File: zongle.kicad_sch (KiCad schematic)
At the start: 20 parts, among them U1 453-00059R

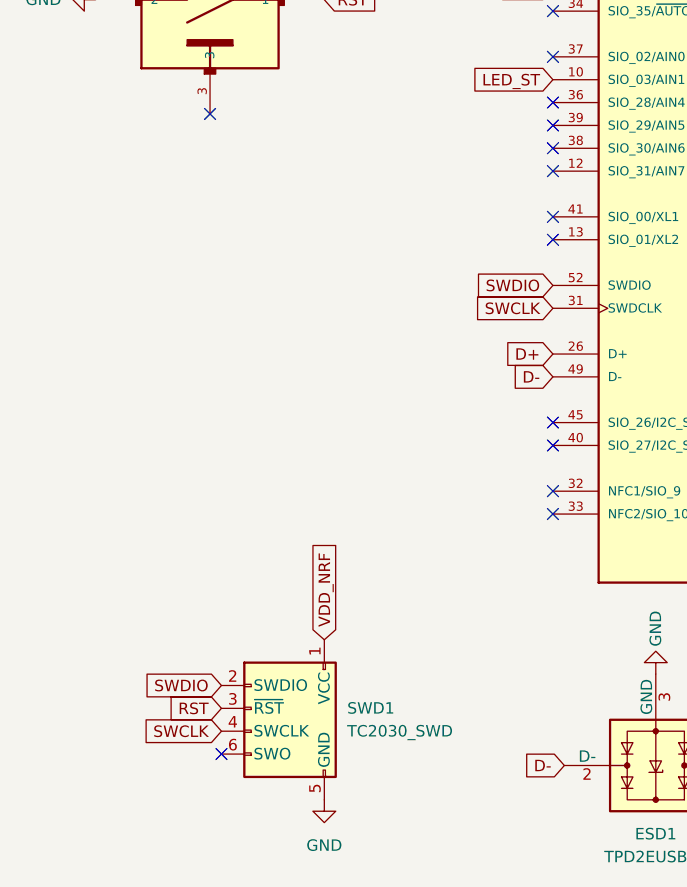
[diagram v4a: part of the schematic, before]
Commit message: some routing cleanup, some drc fixes, assigned parts to every footprint
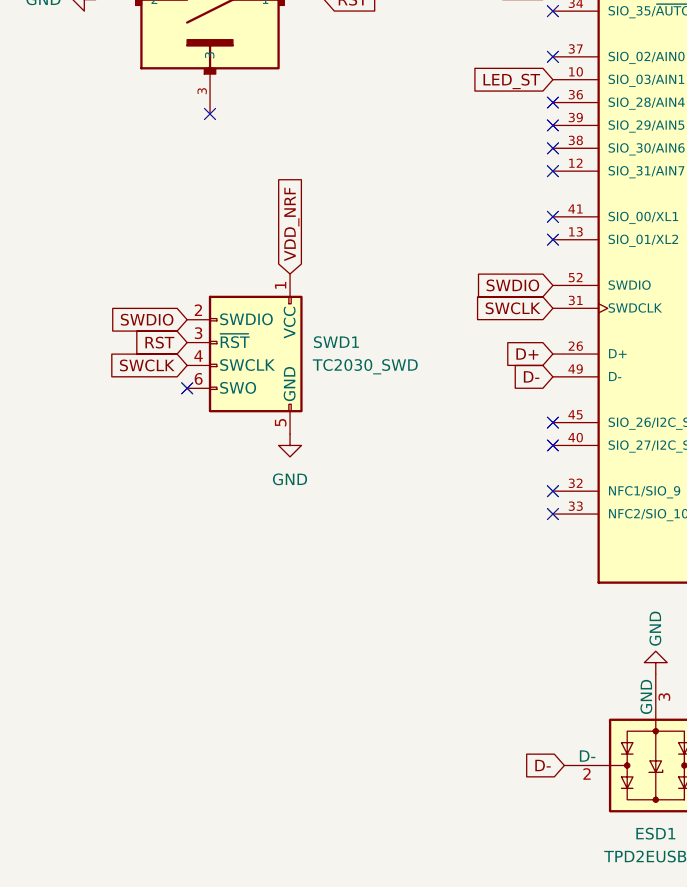
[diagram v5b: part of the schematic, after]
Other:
- moved on the sheet: SWD1
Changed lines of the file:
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@@
 	)
 	(no_connect
-		(at 34.29 149.86)
+		(at 30.48 109.22)
 	)
 	(no_connect
@@
 	(global_label "RST"
 		(shape input)
-		(at 34.29 144.78 180)
-		(fields_autoplaced yes)
-		(effects
-			(font
-				(size 1.27 1.27)
-			)
-			(justify right)
-		)
-		(property "Intersheetrefs" "${INTERSHEET_REFS}"
-			(at 27.8577 144.78 0)
+		(at 30.48 104.14 180)
+		(fields_autoplaced yes)
+		(effects
+			(font
+				(size 1.27 1.27)
+			)
+			(justify right)
+		)
+		(property "Intersheetrefs" "${INTERSHEET_REFS}"
+			(at 24.0477 104.14 0)
 			(effects
 				(font
@@
 	(global_label "SWCLK"
 		(shape input)
-		(at 34.29 147.32 180)
-		(fields_autoplaced yes)
-		(effects
-			(font
-				(size 1.27 1.27)
-			)
-			(justify right)
-		)
-		(property "Intersheetrefs" "${INTERSHEET_REFS}"
-			(at 25.0758 147.32 0)
+		(at 30.48 106.68 180)
+		(fields_autoplaced yes)
+		(effects
+			(font
+				(size 1.27 1.27)
+			)
+			(justify right)
+		)
+		(property "Intersheetrefs" "${INTERSHEET_REFS}"
+			(at 21.2658 106.68 0)
 			(effects
 				(font
@@
 	(global_label "VDD_NRF"
 		(shape input)
-		(at 45.72 137.16 90)
+		(at 41.91 96.52 90)
 		(fields_autoplaced yes)
 		(effects
@@
 		)
 		(property "Intersheetrefs" "${INTERSHEET_REFS}"
-			(at 45.72 125.8895 90)
+			(at 41.91 85.2495 90)
 			(effects
 				(font
@@
 	(global_label "SWDIO"
 		(shape input)
-		(at 34.29 142.24 180)
-		(fields_autoplaced yes)
-		(effects
-			(font
-				(size 1.27 1.27)
-			)
-			(justify right)
-		)
-		(property "Intersheetrefs" "${INTERSHEET_REFS}"
-			(at 25.4386 142.24 0)
+		(at 30.48 101.6 180)
+		(fields_autoplaced yes)
+		(effects
+			(font
+				(size 1.27 1.27)
+			)
+			(justify right)
+		)
+		(property "Intersheetrefs" "${INTERSHEET_REFS}"
+			(at 21.6286 101.6 0)
 			(effects
 				(font
@@
 	(symbol
 		(lib_id "marbastlib-various:TC2030_SWD")
-		(at 40.64 147.32 0)
+		(at 36.83 106.68 0)
 		(unit 1)
 		(exclude_from_sim no)
@@
 		(fields_autoplaced yes)
 		(property "Reference" "SWD1"
-			(at 48.26 144.7799 0)
+			(at 44.45 104.1399 0)
 			(effects
 				(font
@@
 		)
 		(property "Value" "TC2030_SWD"
-			(at 48.26 147.3199 0)
+			(at 44.45 106.6799 0)
 			(effects
 				(font
@@
 		)
 		(property "Footprint" "marbastlib-various:CON_TC2030_outlined"
-			(at 50.8 146.05 90)
+			(at 46.99 105.41 90)
 			(effects
 				(font
@@
 		)
 		(property "Datasheet" "~"
-			(at 8.255 161.29 0)
+			(at 4.445 120.65 0)
 			(effects
 				(font
@@
 		)
 		(property "Description" "6-pin TC2030 connector for SWD programming"
-			(at 40.64 147.32 0)
+			(at 36.83 106.68 0)
 			(effects
 				(font
@@
 	(symbol
 		(lib_id "power:GND")
-		(at 45.72 154.94 0)
+		(at 41.91 114.3 0)
 		(unit 1)
 		(exclude_from_sim no)
@@
 		(fields_autoplaced yes)
 		(property "Reference" "#PWR07"
-			(at 45.72 161.29 0)
+			(at 41.91 120.65 0)
 			(effects
 				(font
@@
 		)
 		(property "Value" "GND"
-			(at 45.72 160.02 0)
+			(at 41.91 119.38 0)
 			(effects
 				(font
@@
 		)
 		(property "Footprint" ""
-			(at 45.72 154.94 0)
+			(at 41.91 114.3 0)
 			(effects
 				(font
@@
 		)
 		(property "Datasheet" ""
-			(at 45.72 154.94 0)
+			(at 41.91 114.3 0)
 			(effects
 				(font
@@
 		)
 		(property "Description" "Power symbol creates a global label with name \"GND\" , ground"
-			(at 45.72 154.94 0)
-			(effects
-				(font
+			(at 41.91 114.3 0)
+			(effects
+				(font

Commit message: minor changes to the routing. final tweaks for first version
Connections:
- no-connect marks 44 -> 43
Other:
- moved on the sheet: C22, C26, ESD1, F1, FB1, LED_STATUS1, R21, R23, R26, SWD1, SWReset_1, Tp+5v1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

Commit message: linked model for 453-00059 nrf52833 module, later will move all the modules to the project repo, so that using this on another device is possible without new linking of the models
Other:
- title: (none) -> zongle
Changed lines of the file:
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@@
 	(generator_version "9.0")
 	(paper "A4")
+	(title_block
+		(title "zongle")
+		(date "2025-12-10")
+		(rev "0.0.2")
+	)
 	(junction
 		(at 185.42 123.19)

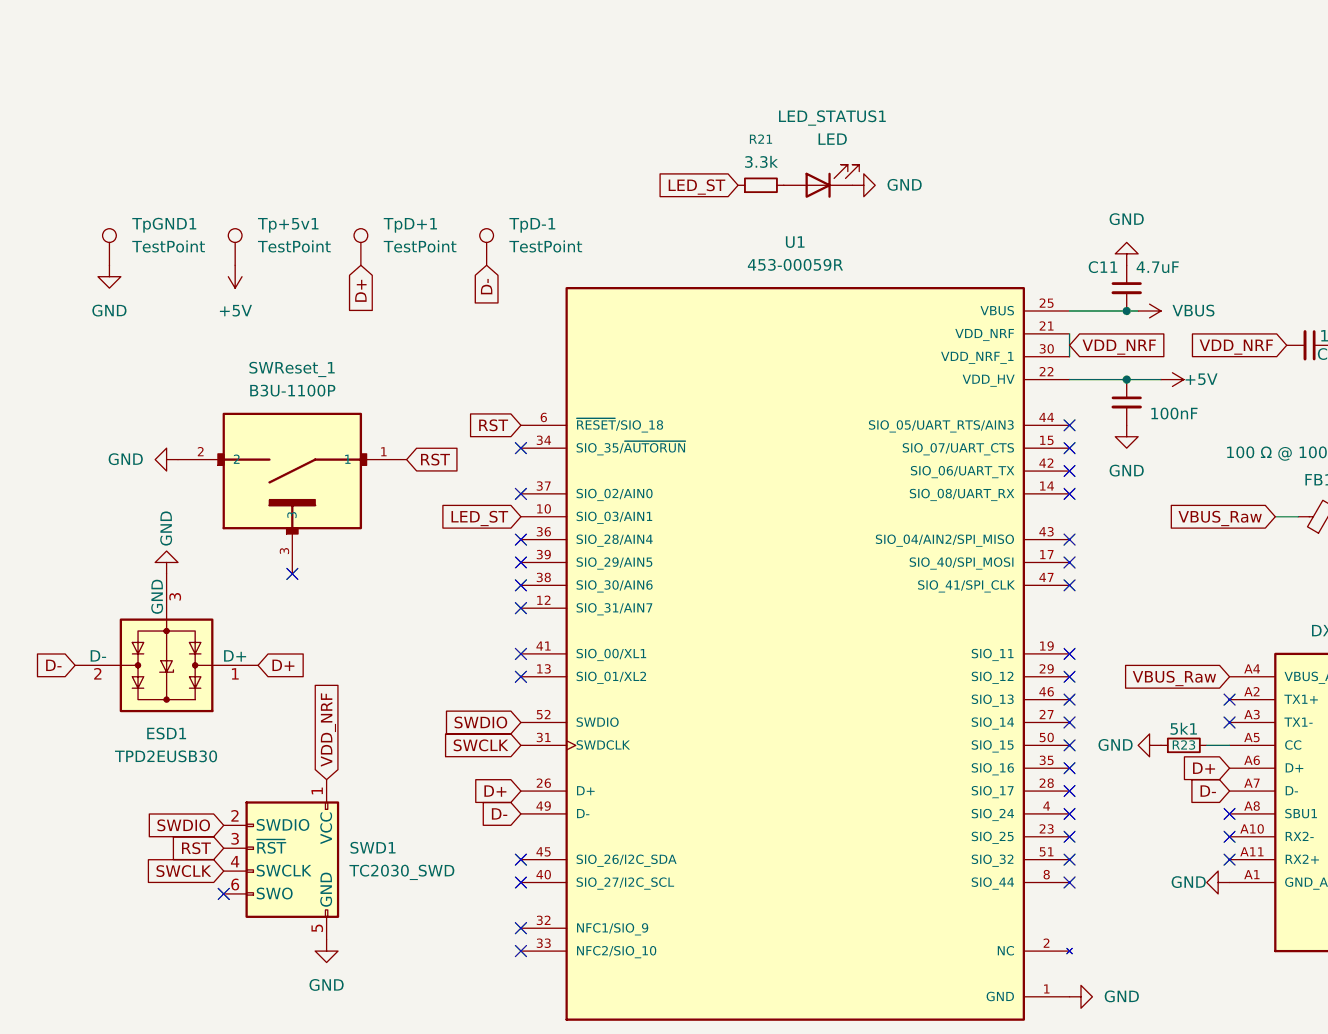
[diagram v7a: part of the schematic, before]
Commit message: moved led outside of antenna perimeter just to be extra sure. some via stitching + cleanup
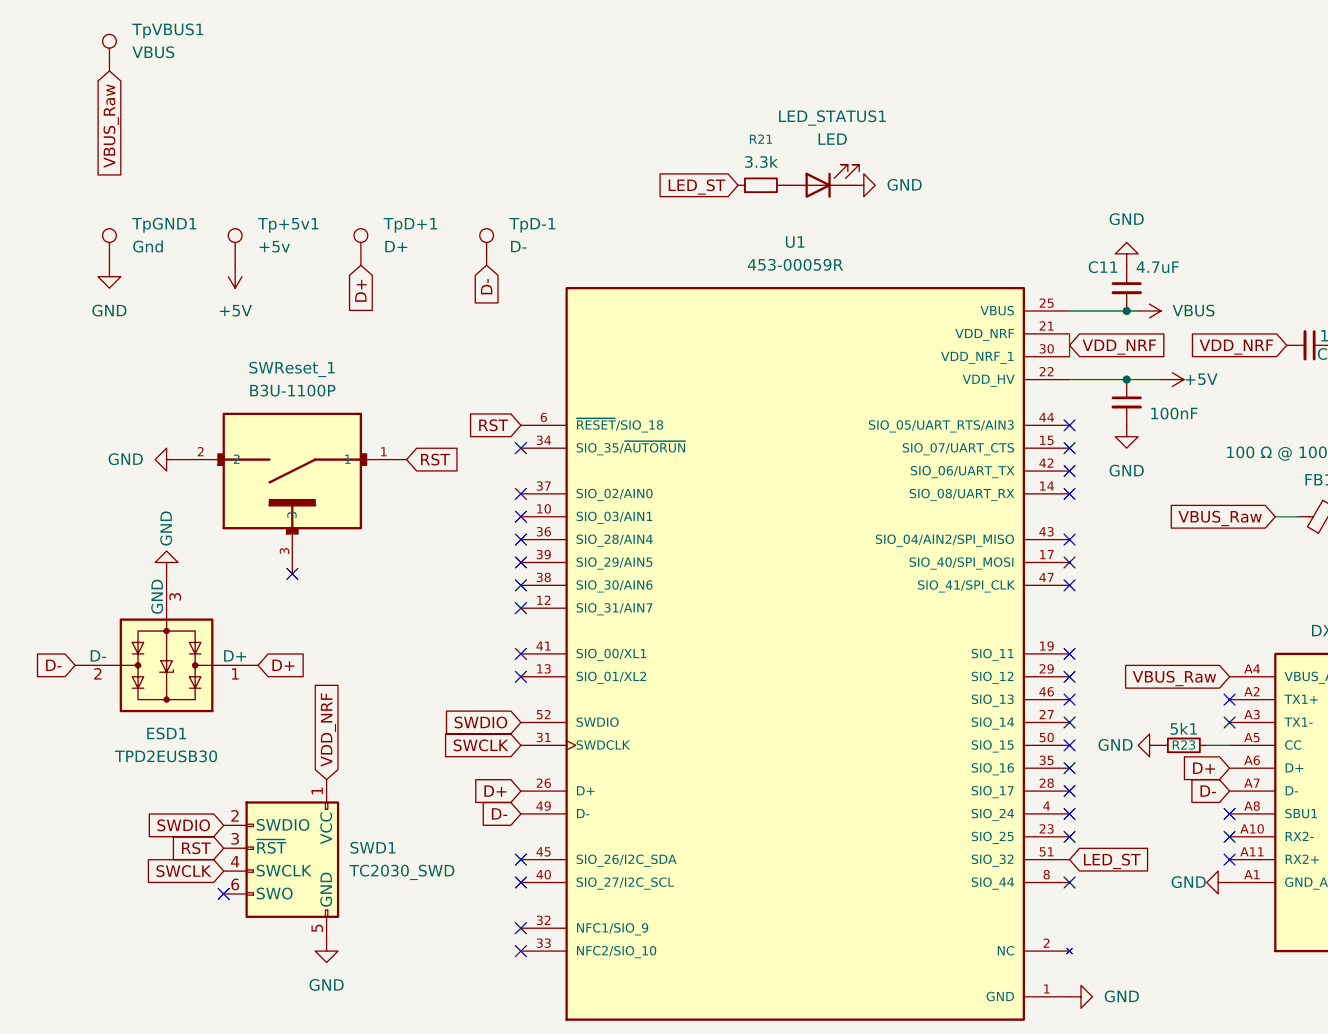
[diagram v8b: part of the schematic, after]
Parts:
- added TpVBUS1: VBUS, TestPoint:TestPoint_Pad_1.0x1.0mm, symbol Connector:TestPoint
- Tp+5v1: value TestPoint -> +5v
- TpD+1: value TestPoint -> D+
- TpD-1: value TestPoint -> D-
- TpGND1: value TestPoint -> Gnd
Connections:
- net LED_ST: now also U1.51 (SIO_32); no longer U1.10 (SIO_03/AIN1)
- net VBUS_A: now also TpVBUS1.1
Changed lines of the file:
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@@
 	)
 	(no_connect
-		(at 132.08 113.03)
-	)
-	(no_connect
 		(at 185.42 95.25)
 	)
@@
 	)
 	(no_connect
+		(at 71.12 74.93)
+	)
+	(no_connect
 		(at 71.12 90.17)
 	)
@@
 	(global_label "LED_ST"
 		(shape input)
-		(at 71.12 74.93 180)
+		(at 132.08 113.03 0)
 		(fields_autoplaced yes)
 		(effects
@@
 				(size 1.27 1.27)
 			)
-			(justify right)
+			(justify left)
 		)
 		(property "Intersheetrefs" "${INTERSHEET_REFS}"
-			(at 61.543 74.93 0)
+			(at 141.657 113.03 0)
 			(effects
 				(font
 					(size 1.27 1.27)
 				)
-				(justify right)
+				(justify left)
 				(hide yes)
 			)
@@
 		)
 	)
+	(global_label "VBUS_Raw"
+		(shape input)
+		(at 25.4 25.4 270)
+		(fields_autoplaced yes)
+		(effects
+			(font
+				(size 1.27 1.27)
+			)
+			(justify right)
+		)
+		(property "Intersheetrefs" "${INTERSHEET_REFS}"
+			(at 25.4 38.0009 90)
+			(effects
+				(font
+					(size 1.27 1.27)
+				)
+				(justify right)
+				(hide yes)
+			)
+		)
+	)
 	(global_label "D-"
 		(shape input)
@@
 			)
 		)
-		(property "Value" "TestPoint"
+		(property "Value" "D-"
 			(at 69.85 44.9579 0)
 			(effects
@@
 			)
 		)
-		(property "Value" "TestPoint"
+		(property "Value" "+5v"
 			(at 41.91 44.9579 0)
 			(effects
@@
 			)
 		)
-		(property "Value" "TestPoint"
+		(property "Value" "D+"
 			(at 55.88 44.9579 0)
 			(effects
@@
 			)
 		)
-		(property "Value" "TestPoint"
+		(property "Value" "Gnd"
 			(at 27.94 44.9579 0)
 			(effects
@@
 					(unit 1)
 				)
+			)
+		)
+	)
+	(symbol
+		(lib_id "Connector:TestPoint")
+		(at 25.4 25.4 0)
+		(unit 1)
+		(exclude_from_sim no)
+		(in_bom yes)
+		(on_board yes)
+		(dnp no)
+		(fields_autoplaced yes)
+		(property "Reference" "TpVBUS1"
+			(at 27.94 20.8279 0)
+			(effects
+				(font
+					(size 1.27 1.27)
+				)
+				(justify left)
+			)
+		)
+		(property "Value" "VBUS"
+			(at 27.94 23.3679 0)
+			(effects
+				(font
+					(size 1.27 1.27)
+				)
+				(justify left)
+			)
+		)
+		(property "Footprint" "TestPoint:TestPoint_Pad_1.0x1.0mm"
+			(at 30.48 25.4 0)
+			(effects
+				(font
+					(size 1.27 1.27)
+				)
+				(hide yes)
+			)
+		)
+		(property "Datasheet" "~"
+			(at 30.48 25.4 0)
+			(effects
+				(font
+					(size 1.27 1.27)
+				)
+				(hide yes)
+			)
+		)
+		(property "Description" "test point"
+			(at 25.4 25.4 0)
+			(effects
+				(font
+					(size 1.27 1.27)
+				)
+				(hide yes)
+			)
+		)
+		(pin "1"
+		)
+		(instances
+			(project "zongle"
+				(path "/e563ac8d-b93c-431b-8d13-48f254367838"
+					(reference "TpVBUS1")
+					(unit 1)
+				)
